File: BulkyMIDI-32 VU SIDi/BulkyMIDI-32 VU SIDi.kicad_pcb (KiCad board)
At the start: 2 copper layers, 100 x 100 mm, 106 parts, among them J1 DC IN, J12 SERIAL, J13 ICSP, J2 MIDI THRU, J3 MIDI IN, J4 Panel, J5 VU INPUT, J6 Power, J8 SID, J9 VU OUTPUT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

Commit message: Moved components in the way of mounting panel
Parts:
- moved R21 39.0 mm to (122.6, 132.1), turned to 90 degrees
- moved RV1 3.18 mm to (162.1, 135.3)
- moved RV3 2.54 mm to (162.1, 122.6)
- moved C13 1.27 mm to (154.9, 128.3)
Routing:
- net /ACT: track 17.5 -> 57.7 mm, vias 0 -> 1
- net Net-(Q3-Pad3): track 28.2 -> 41.3 mm
- net Net-(Q1-Pad1): track 45.8 -> 52.9 mm
- net /R1: track 26.3 -> 23.7 mm
- net Net-(RV3-Pad2): track 190.3 -> 192.8 mm
- net Net-(RV3-Pad5): track 188.7 -> 191.3 mm
- net Net-(C5-Pad1): track 81.2 -> 79.6 mm
- net Net-(C8-Pad1): track 35.3 -> 34.0 mm
- net Net-(C13-Pad1): track 88.9 -> 87.6 mm
- net /R2: track 32.8 -> 31.7 mm
- net Net-(C19-Pad2): track 5.36 -> 6.41 mm
- net /L10: track 27.5 -> 28.4 mm
- net Net-(Q1-Pad2): track 9.42 -> 8.55 mm
- net Net-(C13-Pad2): track 17.5 -> 18.0 mm
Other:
- board text added: "BulkyMIDI-32 VU SIDi (rev. B) github.com/tebl"
- board text removed: "BulkyMIDI-32 VU SIDi (rev. A) github.com/tebl"

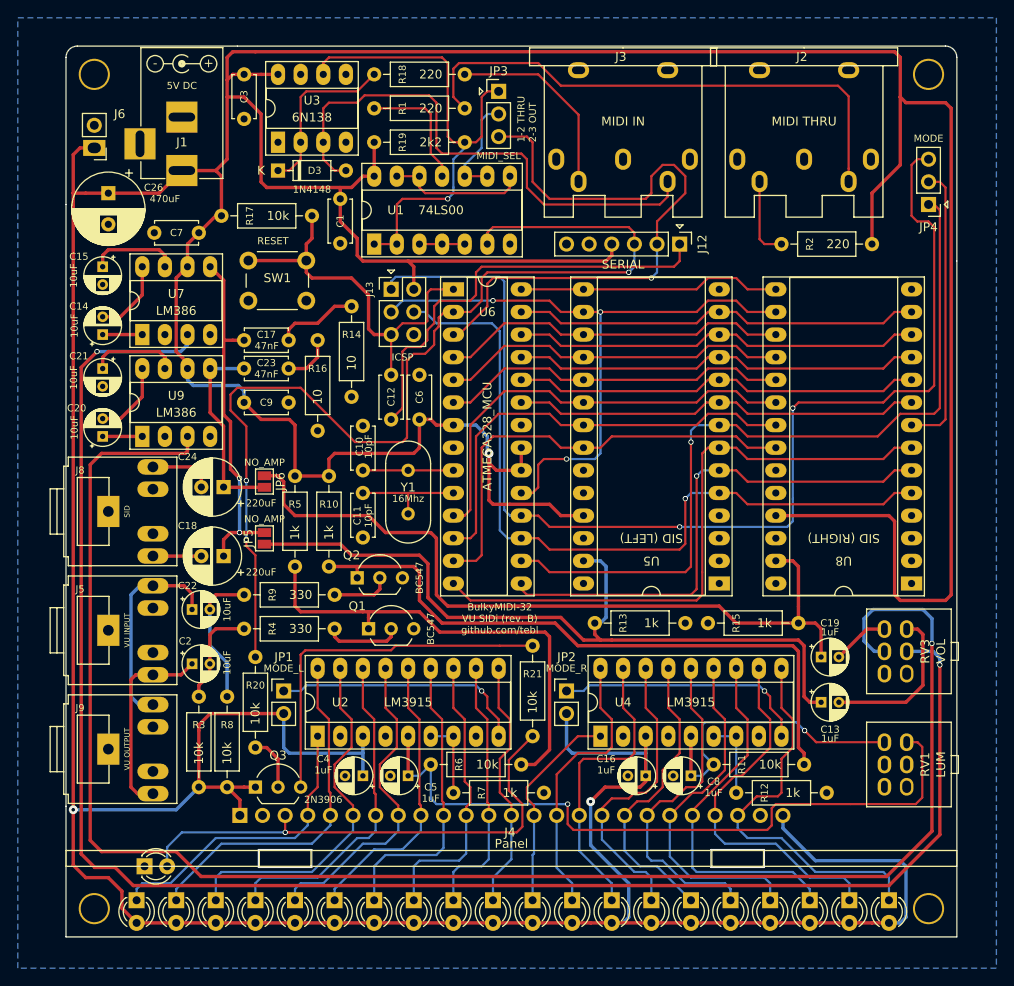
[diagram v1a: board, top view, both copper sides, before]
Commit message: Moved audio jacks slightly
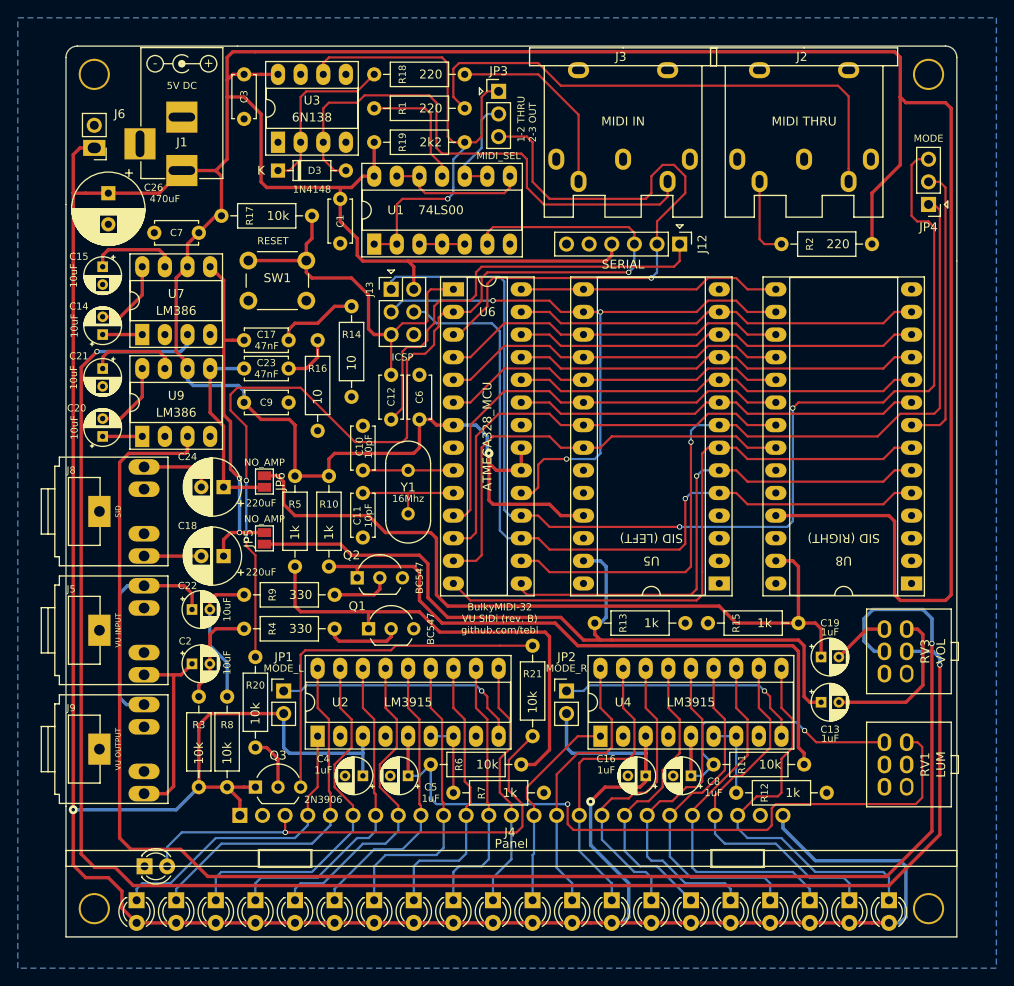
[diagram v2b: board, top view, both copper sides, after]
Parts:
- moved J5 1.00 mm to (75.5, 120.2)
- moved J8 1.00 mm to (75.5, 106.8)
- moved J9 1.00 mm to (75.5, 133.5)
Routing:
- net Net-(RV3-Pad5): track 191.3 -> 184.7 mm
- net /SID_L: track 5.44 -> 7.44 mm
- net VU_R: track 23.7 -> 25.4 mm
- net /SID_R: track 7.31 -> 8.31 mm
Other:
- board text added: "MIDI THRU (MCU)"
- board text removed: "MIDI OUT (MCU)"

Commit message: Increase C4/C16 capacity slightly
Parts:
- C16, C4: value 1uF -> 10uF

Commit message: Simpler VU meter circuit
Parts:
- removed C2, C22: 10uF, Capacitor_THT:CP_Radial_D4.0mm_P2.00mm
- removed C5, C8: 1uF, Capacitor_THT:CP_Radial_D4.0mm_P2.00mm
- removed JP1: MODE_L, Connector_PinHeader_2.54mm:PinHeader_1x02_P2.54mm_Vertical
- removed JP2: MODE_R, Connector_PinHeader_2.54mm:PinHeader_1x02_P2.54mm_Vertical
- removed Q1, Q2: BC547, Package_TO_SOT_THT:TO-92_Inline_Wide
- removed R10: 1k, resistor:R_Axial_DIN0207_L6.3mm_D2.5mm_P10.16mm_Horizontal
- removed R11: 10k, resistor:R_Axial_DIN0207_L6.3mm_D2.5mm_P10.16mm_Horizontal
- R4: value 330 -> 560
- R5: value 1k -> 20k
- R8: value 10k -> 560
- R9: value 330 -> 20k
- moved R9 56.0 mm to (153.0, 135.3)
- moved R8 44.9 mm to (129.5, 120.0), turned to 0 degrees
- moved R5 41.2 mm to (121.3, 135.3), turned to 180 degrees
- moved R21 28.0 mm to (94.6, 133.3)
- moved R6 23.6 mm to (87.6, 133.3), turned to 90 degrees
- moved R13 8.45 mm to (124.8, 112.4), turned to 90 degrees
- moved R3 4.49 mm to (84.5, 133.3)
- moved R4 0.90 mm to (99.7, 120.7), turned to 0 degrees
- moved R15 0.64 mm to (152.4, 120.0)
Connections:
- R3 pad 1: +5V -> Net-(R3-Pad1)
- R3 pad 2: Net-(C2-Pad2) -> VU_L
- R4 pad 1: Net-(Q1-Pad2) -> GND
- R4 pad 2: Net-(C2-Pad2) -> Net-(R4-Pad2)
- R5 pad 2: Net-(Q1-Pad1) -> Net-(R4-Pad2)
- R6 pad 1: Net-(C5-Pad1) -> Net-(R6-Pad1)
- R6 pad 2: Net-(Q1-Pad1) -> VU_R
- R8 pad 1: +5V -> GND
- R8 pad 2: Net-(C22-Pad2) -> Net-(R8-Pad2)
- R9 pad 1: Net-(Q2-Pad2) -> +5V
- R9 pad 2: Net-(C22-Pad2) -> Net-(R8-Pad2)
- RV1 pad 1: GND -> Net-(R3-Pad1)
- RV1 pad 2: GND -> Net-(RV1-Pad2)
- RV1 pad 3: Net-(C5-Pad1) -> GND
- RV1 pad 4: GND -> Net-(R6-Pad1)
- RV1 pad 5: GND -> Net-(RV1-Pad5)
- RV1 pad 6: Net-(C8-Pad1) -> GND
- U2 pad 5: Net-(C5-Pad1) -> Net-(RV1-Pad2)
- U2 pad 6: Net-(R7-Pad1) -> Net-(R4-Pad2)
- U2 pad 9: Net-(JP1-Pad1) -> +5V
- U4 pad 5: Net-(C8-Pad1) -> Net-(RV1-Pad5)
- U4 pad 6: Net-(R12-Pad1) -> Net-(R8-Pad2)
- U4 pad 9: Net-(JP2-Pad1) -> +5V
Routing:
- net Net-(R3-Pad1): track 0.00 -> 99.1 mm
- net Net-(R6-Pad1): track 0.00 -> 93.8 mm
- net Net-(C5-Pad1): track 79.6 -> 0.00 mm, vias 1 -> 0
- net Net-(RV1-Pad2): track 0.00 -> 77.6 mm, vias 0 -> 1
- net Net-(Q2-Pad1): track 72.7 -> 0.00 mm
- net Net-(Q1-Pad1): track 52.9 -> 0.00 mm
- net Net-(C8-Pad1): track 34.0 -> 0.00 mm, vias 1 -> 0
- net /ACT: track 57.7 -> 24.5 mm, vias 1 -> 0
- net Net-(JP2-Pad1): track 28.6 -> 0.00 mm, vias 1 -> 0
- net Net-(JP1-Pad1): track 28.6 -> 0.00 mm, vias 1 -> 0
- net Net-(Q3-Pad3): track 41.3 -> 15.4 mm
- net Net-(RV1-Pad5): track 0.00 -> 25.4 mm, vias 0 -> 1
- net Net-(R8-Pad2): track 0.00 -> 16.6 mm
- net Net-(C22-Pad2): track 15.7 -> 0.00 mm
- net Net-(R4-Pad2): track 0.00 -> 15.1 mm
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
